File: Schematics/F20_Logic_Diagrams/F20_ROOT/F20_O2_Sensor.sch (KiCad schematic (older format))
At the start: 2 parts, among them U3 O2_Sensor

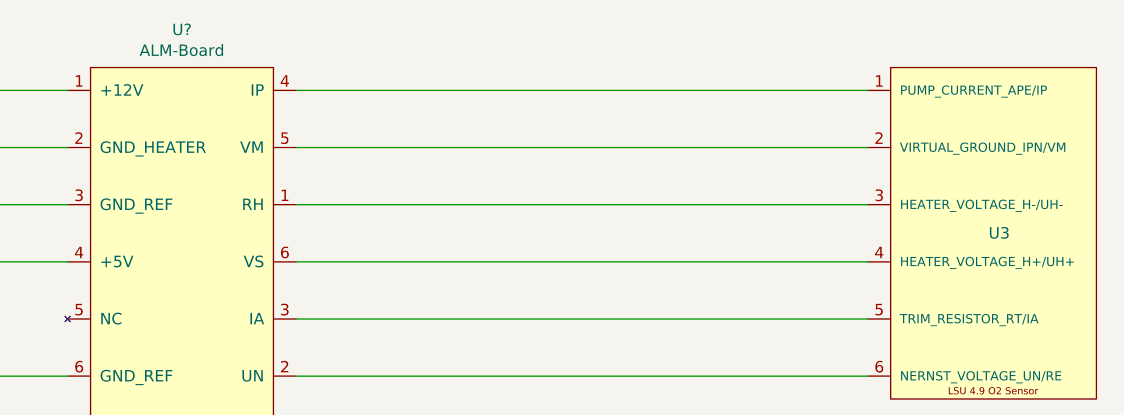
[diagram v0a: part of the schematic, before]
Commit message: Re-annotated Logic Diagrams, pulled a BOM list based on Logic Diagrams
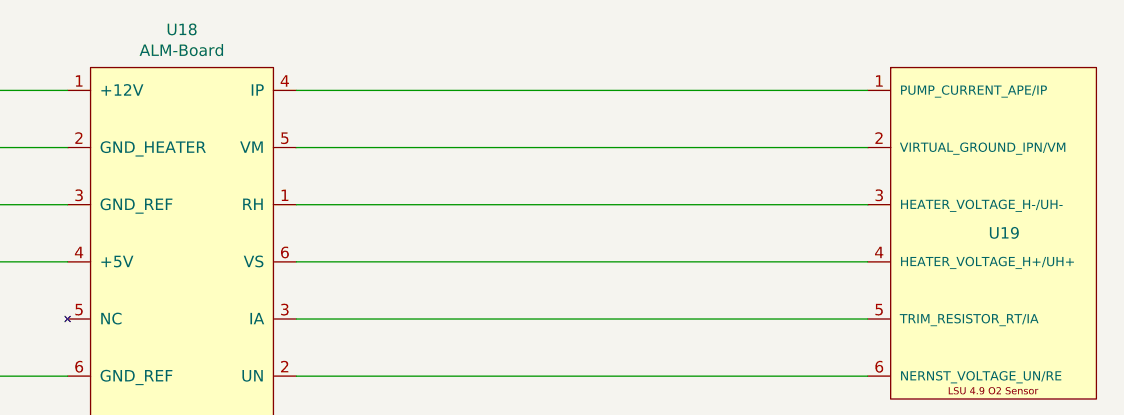
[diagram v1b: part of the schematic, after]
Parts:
- gave numbers to parts that had none: 1
- renumbered U3 to U19
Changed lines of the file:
@@
 $EndDescr
 $Comp
-L FSAE_Library:O2_Sensor U3
+L FSAE_Library:O2_Sensor U19
 U 1 1 5E390A68
 P 8500 2500
-F 0 "U3" H 9028 1875 50  0000 L CNN
+F 0 "U19" H 9028 1875 50  0000 L CNN
 F 1 "O2_Sensor" H 8800 2650 50  0001 C CNN
 F 2 "" H 8800 2650 50  0001 C CNN
@@
 Heater 1A typical (1.7A max)\nALM board ~ 60mA
 $Comp
-L FSAE_Library:ALM U?
+L FSAE_Library:ALM U18
 U 1 1 5E77730D
 P 5000 2500
-F 0 "U?" H 5500 2765 50  0000 C CNN
+F 0 "U18" H 5500 2765 50  0000 C CNN
 F 1 "ALM" H 5300 2650 50  0001 C CNN
 F 2 "" H 5300 2650 50  0001 C CNN
@@
 	2500 4250 5000 4250
 $Comp
-L FSAE_Library:GND #PWR?
+L FSAE_Library:GND #PWR013
 U 1 1 5E794BC7
 P 4000 5000
-F 0 "#PWR?" H 4000 4800 50  0001 C CNN
+F 0 "#PWR013" H 4000 4800 50  0001 C CNN
 F 1 "GND" H 4004 4846 50  0000 C CNN
 F 2 "" H 4000 4950 50  0001 C CNN
@@
 $EndComp
 $Comp
-L FSAE_Library:GND_BAT #PWR?
+L FSAE_Library:GND_BAT #PWR014
 U 1 1 5E795446
 P 4500 5000
-F 0 "#PWR?" H 4500 4750 50  0001 C CNN
+F 0 "#PWR014" H 4500 4750 50  0001 C CNN
 F 1 "GND_BAT" H 4505 4827 50  0000 C CNN
 F 2 "" H 4500 5000 50  0001 C CNN
